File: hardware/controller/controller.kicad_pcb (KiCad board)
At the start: 4 copper layers, 57 x 47 mm, 50 parts, among them J1 Conn_01x02_Pin, J11 Barrel_Jack, J12 USB_C_Receptacle_USB2.0_14P, J2 Conn_01x02_Pin, J3 Conn_01x02_Pin, J5 Screw_Terminal_01x02, J6 Screw_Terminal_01x02, J7 Conn_01x04_Pin, J8 Conn_01x04_Pin, U1 ESP32-C3-MINI-1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

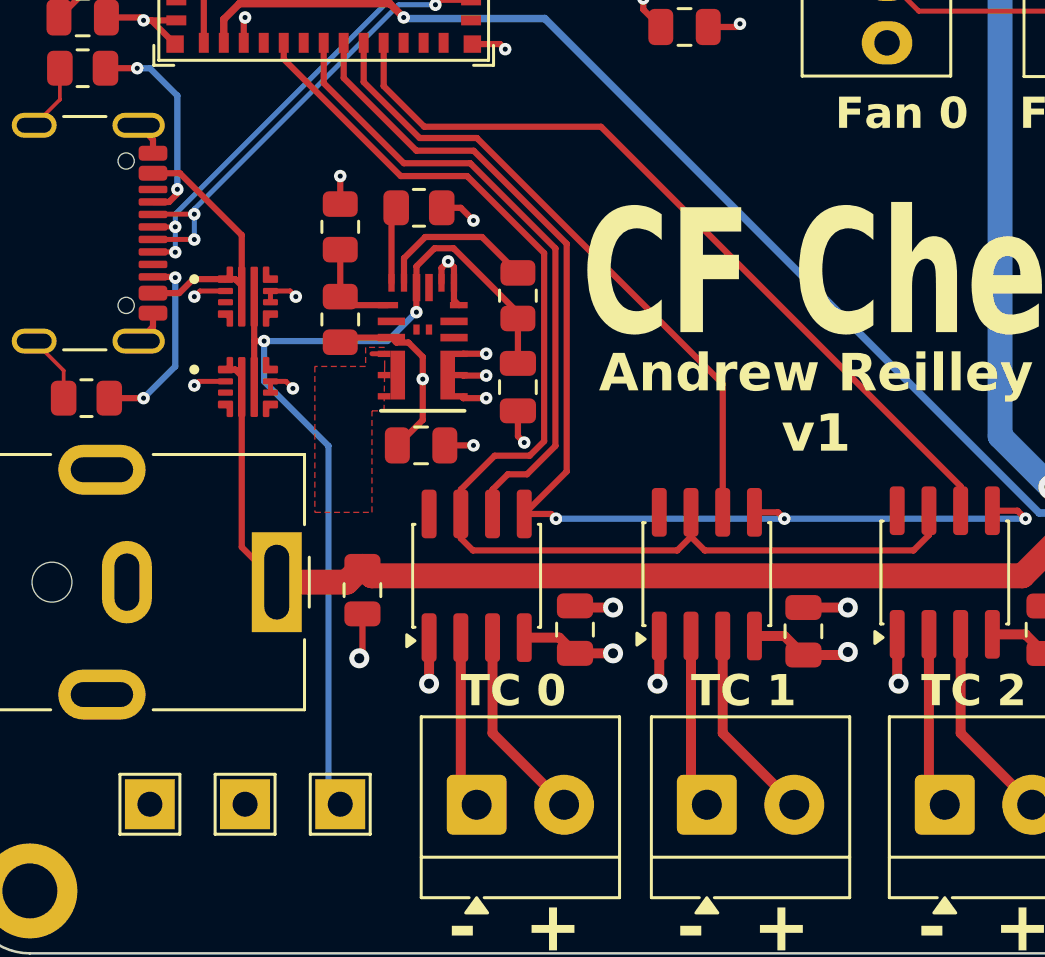
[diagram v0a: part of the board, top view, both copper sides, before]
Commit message: Replace input diodes with power mux chip
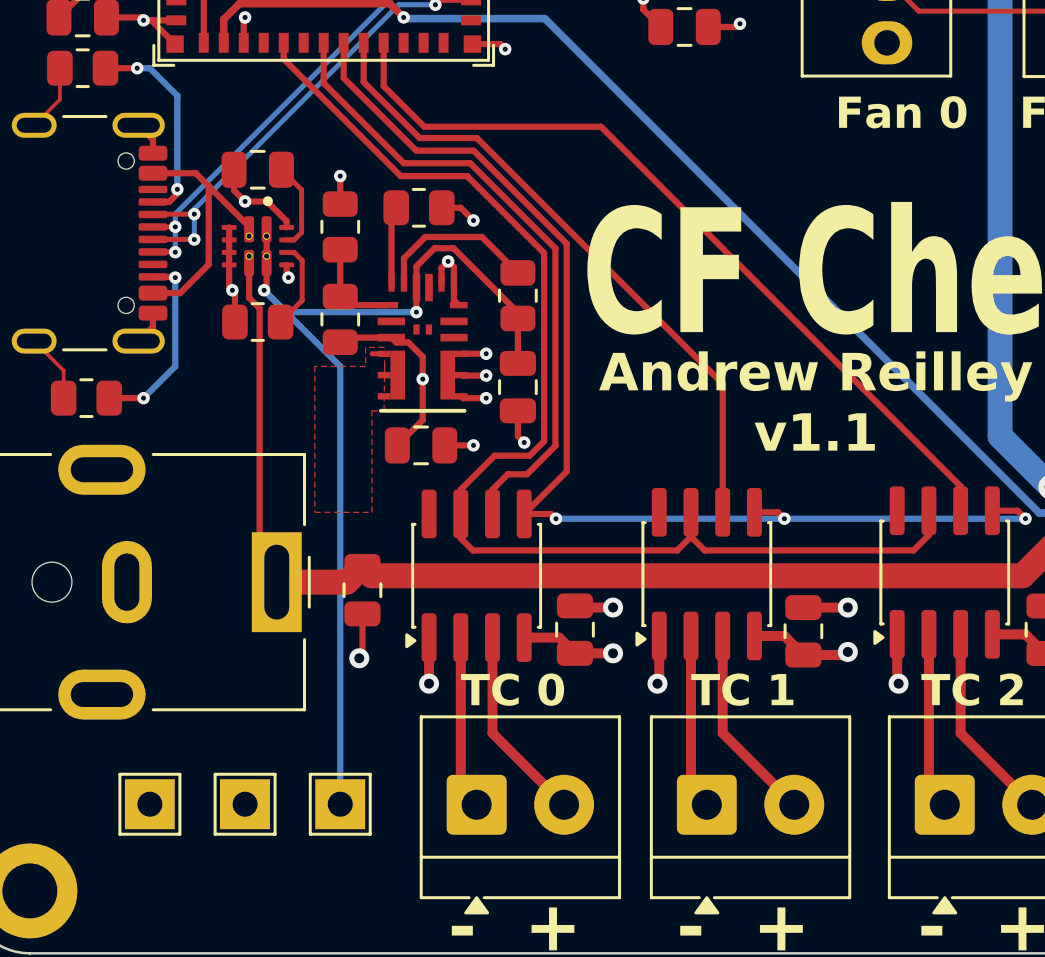
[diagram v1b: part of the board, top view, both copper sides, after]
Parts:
- removed U8, U9: LM73100RPWR, LM73100:IC_LM73100RPWR
- added C5: 0.01uF, Capacitor_SMD:C_0805_2012Metric, F.Cu at (118.9, 87.6)
- added R12: 51.1k, Resistor_SMD:R_0805_2012Metric, F.Cu at (118.9, 93.7)
- added U5: TPS2121RUXR, TPS2121RUXR:IC_TPS2121RUXR, F.Cu at (118.9, 90.7)
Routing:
- net +12V: track 85.6 -> 89.2 mm
- net Net-(U5-ILIM): track 0.00 -> 3.58 mm
- net Net-(U5-SS): track 0.00 -> 3.57 mm
- net GND: track 80.5 -> 83.0 mm, vias 48 -> 47
- net VBUS: track 39.7 -> 40.5 mm
- net +5V: track 11.4 -> 10.7 mm
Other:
- board text added: "Andrew Reilley v1.1"
- board text removed: "Andrew Reilley v1"

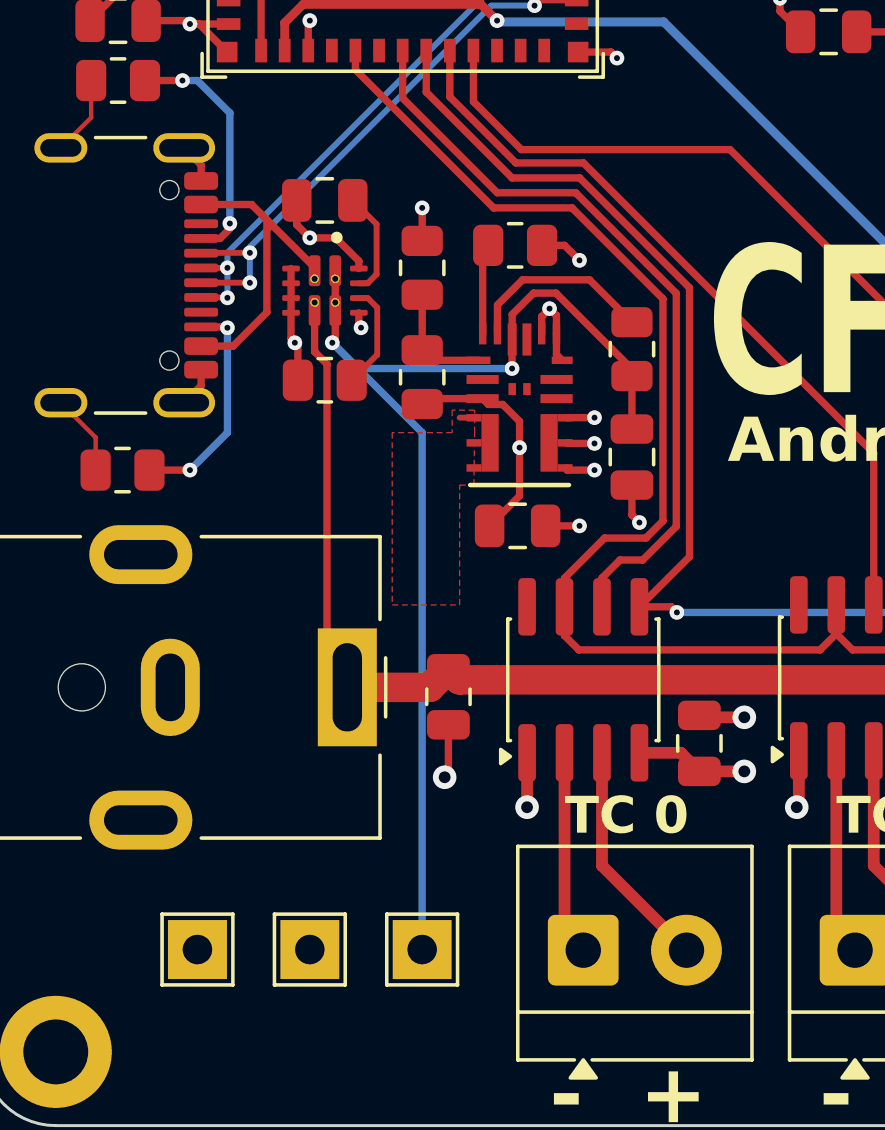
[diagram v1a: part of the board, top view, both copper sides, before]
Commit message: Swap out voltage regulator
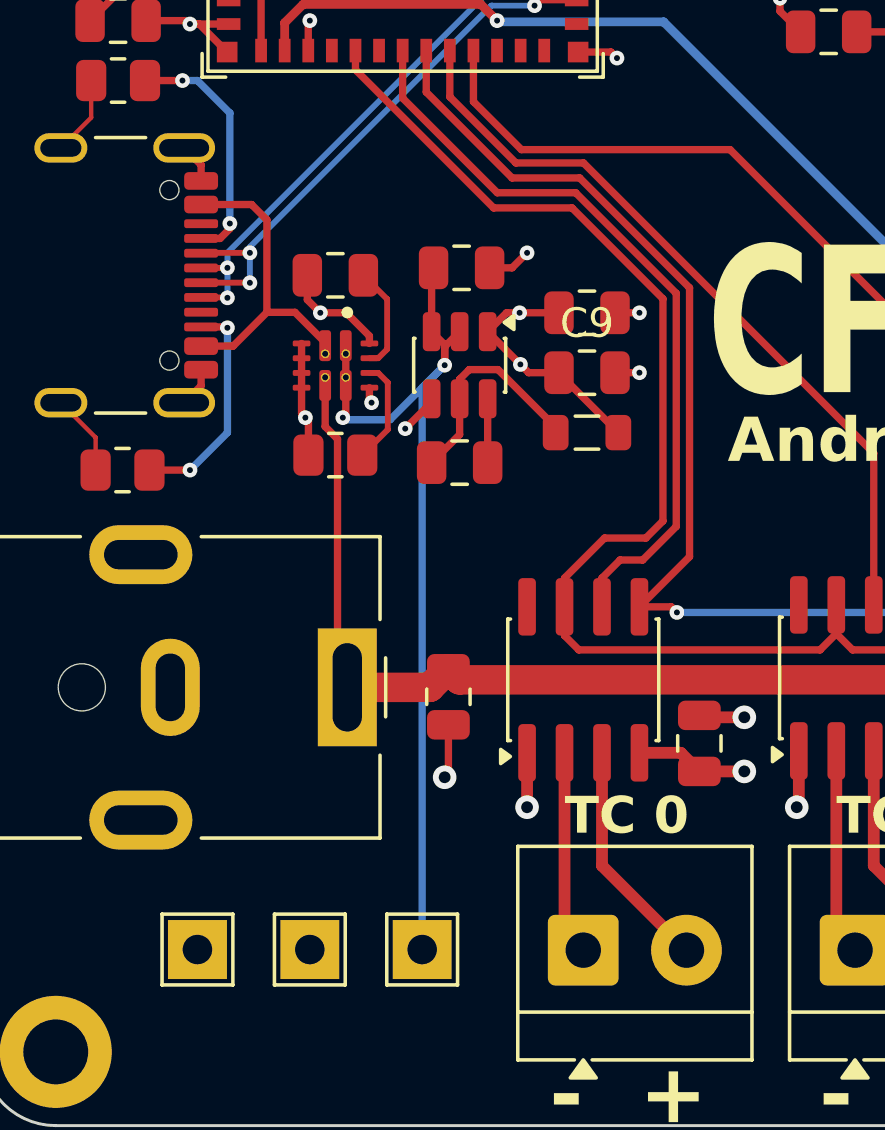
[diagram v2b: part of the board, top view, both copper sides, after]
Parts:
- removed R10: 100k, Resistor_SMD:R_0805_2012Metric
- removed R4: 33k, Resistor_SMD:R_0805_2012Metric
- removed R8: 75k, Resistor_SMD:R_0805_2012Metric
- removed R9: 24k, Resistor_SMD:R_0805_2012Metric
- removed U7: MPM3606AGQV-P, MPM3606:QFN3p0x5p0x1p6_MPM3606A_MNP
- added C13: 100nF, Capacitor_SMD:C_0805_2012Metric, F.Cu at (123.4, 96.5)
- added C9: 22uF, Capacitor_SMD:C_0805_2012Metric, F.Cu at (127.8, 93.5)
- added L1: 3.9uH, Inductor_SMD:L_0805_2012Metric, F.Cu at (127.8, 95.5)
- added U8: AP63203WU, Package_TO_SOT_SMD:TSOT-23-6, F.Cu at (123.4, 93.2)
- C5: value 0.01uF -> 10nF
- moved C11 8.63 mm to (123.5, 89.9), turned to 0 degrees
- moved C10 7.60 mm to (127.8, 91.4), turned to 0 degrees
- moved C5 2.57 mm to (119.2, 90.2)
- moved R12 2.57 mm to (119.2, 96.3)
- moved U5 2.57 mm to (119.2, 93.2)
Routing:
- net GND: track 83.0 -> 74.1 mm
- net VBUS: track 40.5 -> 32.1 mm
- net Net-(U8-SW): track 0.00 -> 7.60 mm
- net Net-(U7-EN): track 6.49 -> 0.00 mm
- net /Power/FB: track 3.93 -> 0.00 mm
- net +3V3: track 28.4 -> 31.5 mm, vias 13 -> 10
- net Net-(U7-PG): track 2.71 -> 0.00 mm
- net Net-(U8-BST): track 0.00 -> 2.16 mm
- net +12V: track 89.2 -> 87.5 mm
- removed copper zone on F.Cu, net /Power/V_SW

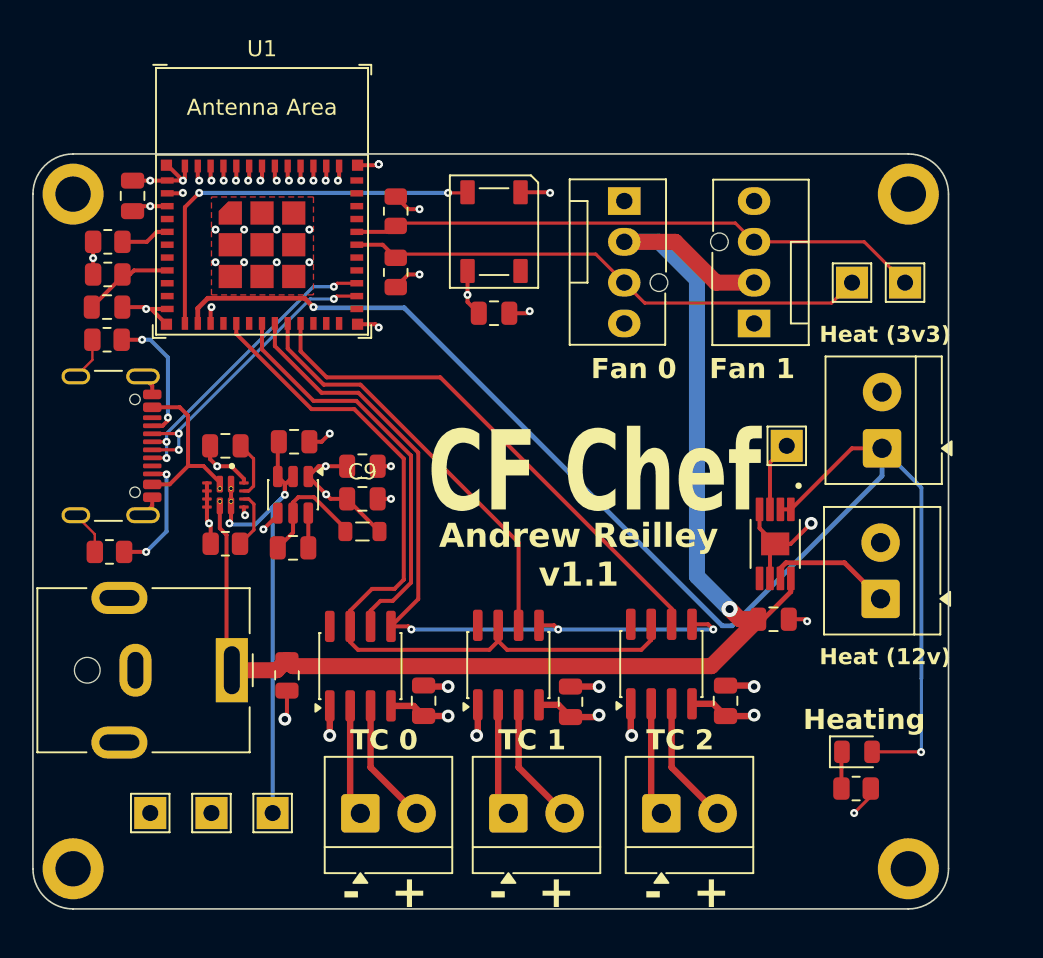
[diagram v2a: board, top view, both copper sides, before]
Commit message: Widen board and add polarity labels to heater outputs
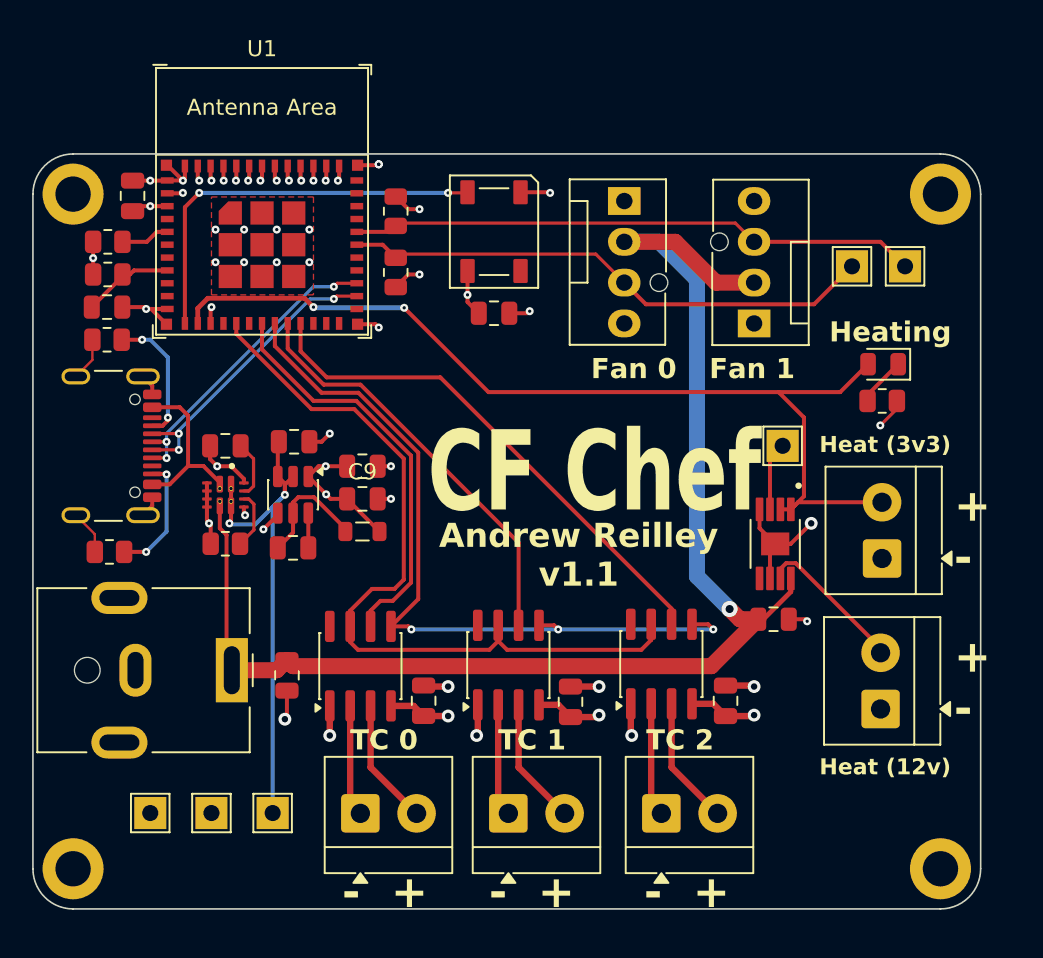
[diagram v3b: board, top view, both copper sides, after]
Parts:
- moved D2 24.2 mm to (160.2, 85.1), turned to 180 degrees
- moved R3 24.2 mm to (160.1, 87.4)
- moved J5 6.86 mm to (160.1, 97.2)
- moved J6 6.86 mm to (160.0, 106.6)
- moved H1 2.00 mm to (163.8, 74.5)
- moved H4 2.00 mm to (163.8, 116.5)
- moved TP4 1.02 mm to (161.5, 79.0)
- moved TP5 1.02 mm to (158.2, 79.0)
- moved TP6 0.25 mm to (153.9, 90.2)
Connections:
- J5 pad 1: /Microcontroller/HEATER -> GND
- J5 pad 2: GND -> /Microcontroller/HEATER
- J6 pad 1: Net-(J6-Pin_1) -> GND
- J6 pad 2: GND -> Net-(J6-Pin_2)
- U6 pad 7: Net-(J6-Pin_1) -> Net-(J6-Pin_2)
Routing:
- net /Microcontroller/HEATER: track 88.8 -> 60.7 mm
- net Net-(J6-Pin_2): track 0.00 -> 9.46 mm
- net Net-(J6-Pin_1): track 7.94 -> 0.00 mm
- net Net-(D2-K): track 2.26 -> 3.08 mm
- net GND: track 74.1 -> 73.5 mm
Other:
- board size 57 x 47 mm -> 59 x 47 mm
- board text added: "+ -"

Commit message: Move 12v out from under TC chips
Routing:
- net +12V: track 87.5 -> 82.7 mm
- net VBUS: track 32.1 -> 33.1 mm
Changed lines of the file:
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@@
-	)
-	(segment
-		(start 144.064 77.47)
-		(end 147.241342 77.47)
-		(width 1)
-		(layer "F.Cu")
-		(net 39)
 	)
 	(segment
@@
 	)
 	(segment
-		(start 147.241342 77.47)
-		(end 149.781342 80.01)
-		(width 1)
-		(layer "F.Cu")
-		(net 39)
-	)
-	(segment
 		(start 152.405 100.965)
 		(end 151.257 100.965)
@@
 		(end 119.3035 103.8095)
 		(width 0.25)
-		(layer "F.Cu")
-		(net 39)
-	)
-	(segment
-		(start 149.781342 80.01)
-		(end 152.146 80.01)
-		(width 1)
 		(layer "F.Cu")
 		(net 39)
@@
 	)
 	(segment
-		(start 123.063 103.51)
-		(end 123.439 103.886)
-		(width 1)
-		(layer "F.Cu")
-		(net 39)
-	)
-	(segment
 		(start 118.946 103.452)
 		(end 119.634 104.14)
@@
 	)
 	(segment
-		(start 123.439 103.886)
-		(end 149.484 103.886)
-		(width 1)
-		(layer "F.Cu")
-		(net 39)
-	)
-	(segment
 		(start 151.257 100.965)
-		(end 150.622 100.33)
-		(width 1)
-		(layer "F.Cu")
-		(net 39)
-	)
-	(segment
-		(start 149.484 103.886)
-		(end 152.405 100.965)
+		(end 148.59 98.298)
 		(width 1)
 		(layer "F.Cu")
@@
 	)
 	(via
-		(at 150.622 100.33)
+		(at 148.59 98.298)
 		(size 1)
 		(drill 0.5)
@@
 	)
 	(segment
+		(start 148.779892 80.01)
+		(end 148.59 79.820108)
+		(width 1)
+		(layer "B.Cu")
+		(net 39)
+	)
+	(segment
+		(start 152.146 80.01)
+		(end 148.779892 80.01)
+		(width 1)
+		(layer "B.Cu")
+		(net 39)
+	)
+	(segment
+		(start 148.59 98.298)
+		(end 125.476 98.298)
+		(width 1)
+		(layer "B.Cu")
+		(net 39)
+	)
+	(segment
 		(start 148.59 79.820108)
 		(end 146.239892 77.47)
@@
 	)
 	(segment
-		(start 150.622 100.33)
-		(end 148.59 98.298)
+		(start 125.476 98.298)
+		(end 119.634 104.14)
 		(width 1)
 		(layer "B.Cu")
@@
 	)
 	(segment
+		(start 122.174 113.03)
+		(end 117.602 108.458)
+		(width 0.25)
+		(layer "B.Cu")
+		(net 45)
+	)
+	(segment
+		(start 117.602 96.8775)
+		(end 119.4835 94.996)
+		(width 0.25)
+		(layer "B.Cu")
+		(net 45)
+	)
+	(segment
 		(start 122.174 93.98)
 		(end 122.936 93.218)
@@
 	)
 	(segment
-		(start 121.702 112.558)
-		(end 122.174 113.03)
-		(width 0.25)
-		(layer "B.Cu")
-		(net 45)
-	)
-	(segment
-		(start 122.174 113.03)
-		(end 122.174 93.98)
-		(width 0.25)
-		(layer "B.Cu")
+		(start 117.602 108.458)
+		(end 117.602 96.8775)
+		(width 0.25)
+		(layer "B.Cu")
